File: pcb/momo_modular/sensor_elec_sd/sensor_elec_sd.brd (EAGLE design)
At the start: 100 x 33 mm, 27 parts, among them U1 AP7115-LDO, U2 16LF1847, U3 TS1100

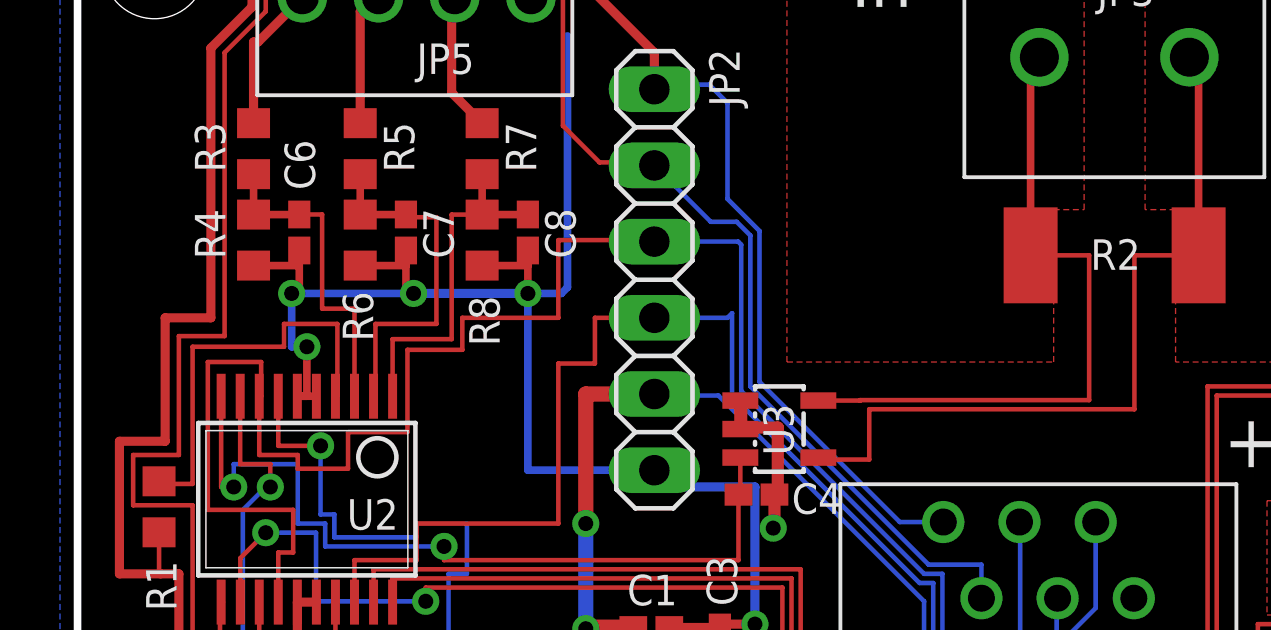
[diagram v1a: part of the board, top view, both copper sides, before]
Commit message: Final changes to sd card and voltage sensing board.
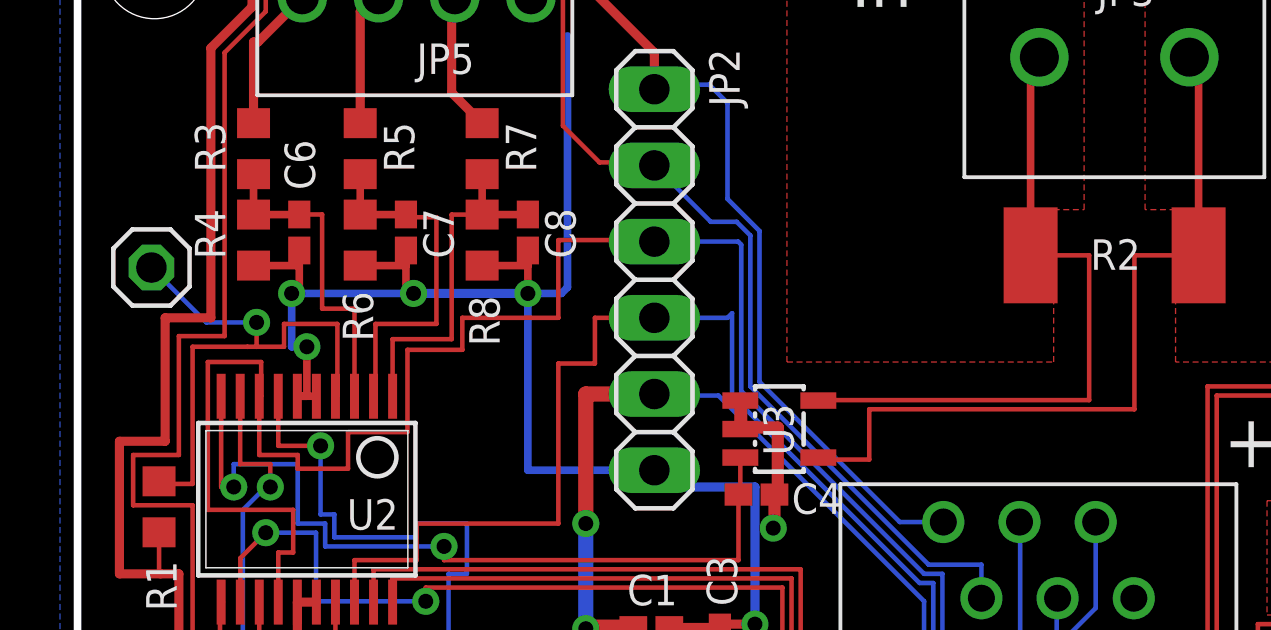
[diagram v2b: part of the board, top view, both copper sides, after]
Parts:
- added JP6: (no value), pinhead:1X01
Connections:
- net N$4: now also JP6.1
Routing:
- net N$4: track 14.1 -> 19.2 mm, vias 0 -> 1
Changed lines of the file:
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@@
 <attribute name="DIGIKEY-PN" value="A98335-ND" x="11.2776" y="33.2232" size="1.016" layer="27" display="off"/>
+</element>
+<element name="JP6" library="pinhead" package="1X01" value="" x="6.2484" y="24.2316" smashed="yes">
+<attribute name="VALUE" x="4.9784" y="21.0566" size="1.27" layer="27"/>
 </element>
 </elements>
@@
 <wire x1="12.446" y1="22.352" x2="10.668" y2="22.352" width="0.1524" layer="1"/>
 <wire x1="10.668" y1="22.352" x2="10.668" y2="21.59" width="0.1524" layer="1"/>
-<wire x1="10.668" y1="21.59" x2="7.62" y2="21.59" width="0.1524" layer="1"/>
+<wire x1="10.668" y1="21.59" x2="9.7536" y2="21.59" width="0.1524" layer="1"/>
+<wire x1="9.4488" y1="21.59" x2="7.62" y2="21.59" width="0.1524" layer="1"/>
 <wire x1="7.62" y1="21.59" x2="7.62" y2="17.018" width="0.1524" layer="1"/>
 <wire x1="7.62" y1="17.018" x2="6.35" y2="17.018" width="0.1524" layer="1"/>
 <wire x1="6.35" y1="17.018" x2="6.5024" y2="17.106" width="0.1524" layer="1"/>
+<contactref element="JP6" pad="1"/>
+<wire x1="6.2484" y1="24.2316" x2="8.0772" y2="22.4028" width="0.1524" layer="16"/>
+<wire x1="8.0772" y1="22.4028" x2="9.7536" y2="22.4028" width="0.1524" layer="16"/>
+<via x="9.7536" y="22.4028" extent="1-16" drill="0.5"/>
+<wire x1="9.7536" y1="22.4028" x2="9.7536" y2="21.59" width="0.1524" layer="1"/>
+<wire x1="9.7536" y1="21.59" x2="9.4488" y2="21.59" width="0.1524" layer="1"/>
 </signal>
 <signal name="SCL">
@@
 <contactref element="U3" pad="5"/>
 <wire x1="37.5056" y1="24.638" x2="35.554" y2="24.638" width="0.1524" layer="1"/>
-<wire x1="28.478" y1="19.7968" x2="29.8704" y2="19.7968" width="0.1524" layer="1"/>
-<wire x1="29.8704" y1="19.7968" x2="29.8704" y2="19.812" width="0.1524" layer="1"/>
-<wire x1="29.8704" y1="19.812" x2="37.5056" y2="19.812" width="0.1524" layer="1"/>
+<wire x1="28.478" y1="19.812" x2="37.5056" y2="19.812" width="0.1524" layer="1"/>
 <wire x1="37.5056" y1="19.812" x2="37.5056" y2="24.638" width="0.1524" layer="1"/>
+<wire x1="28.478" y1="19.812" x2="28.478" y2="19.7968" width="0.1524" layer="1"/>
 </signal>
 <signal name="ISENSE">

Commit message: Finished divider network spec'ing and standardized on 1% resistors to reduce BOM lines.
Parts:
- R3, R5: value (none) -> 620K 1%
- R4, R6, R8: value (none) -> 100K 1%
- R7: value (none) -> 806K 1%
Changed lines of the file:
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@@
 <attribute name="NAME" x="6.0706" y="14.4526" size="1.016" layer="25" rot="R270"/>
 <attribute name="VALUE" x="4.5974" y="16.891" size="1.27" layer="27" rot="R270"/>
-<attribute name="DIGIKEY-PN" value="P10KGCT-ND" x="6.5024" y="16.256" size="1.778" layer="27" rot="R270" display="off"/>
+<attribute name="DIGIKEY-PN" value="P10.0KHCT-ND" x="6.5024" y="16.256" size="1.778" layer="27" rot="R270" display="off"/>
 </element>
 <element name="JP2" library="components" package="1X06" value="MOMO-VERT-6M" x="23.0124" y="21.2852" smashed="yes" rot="R270">
@@
 <attribute name="NAME" x="39.2176" y="25.1714" size="1.016" layer="25" rot="R180"/>
 <attribute name="VALUE" x="40.894" y="27.813" size="1.27" layer="27" rot="R180"/>
-<attribute name="DIGKEY-PN" value="CRF2512-FV-R001ELFCT-ND" x="38.354" y="24.638" size="1.778" layer="27" rot="R180" display="off"/>
+<attribute name="DIGIKEY-PN" value="CRF2512-FV-R001ELFCT-ND" x="38.354" y="24.638" size="1.778" layer="27" rot="R180" display="off"/>
 </element>
 <element name="C4" library="rcl" package="C0402K" value="47 nF" x="26.416" y="16.6624" smashed="yes">
@@
 <attribute name="NAME" x="12.0582" y="11.0156" size="1.016" layer="25" rot="R270"/>
 <attribute name="VALUE" x="9.8784" y="11.168" size="1.016" layer="27" rot="R270"/>
-<attribute name="DIGKIEY-PN" value="445-1265-1-ND" x="11.3284" y="10.668" size="1.778" layer="27" rot="R270" display="off"/>
+<attribute name="DIGIKEY-PN" value="445-1265-1-ND" x="11.3284" y="10.668" size="1.778" layer="27" rot="R270" display="off"/>
 </element>
-<element name="R3" library="rcl" package="R0603" value="" x="9.652" y="28.194" smashed="yes" rot="R90">
+<element name="R3" library="rcl" package="R0603" value="620K 1%" x="9.652" y="28.194" smashed="yes" rot="R90">
 <attribute name="NAME" x="8.7122" y="27.4066" size="1.016" layer="25" rot="R90"/>
 <attribute name="VALUE" x="11.557" y="27.559" size="1.27" layer="27" rot="R90"/>
+<attribute name="DIGIKEY-PN" value="P620KHCT-ND" x="9.652" y="28.194" size="1.778" layer="27" rot="R90" display="off"/>
 </element>
-<element name="R4" library="rcl" package="R0603" value="" x="9.652" y="25.146" smashed="yes" rot="R90">
+<element name="R4" library="rcl" package="R0603" value="100K 1%" x="9.652" y="25.146" smashed="yes" rot="R90">
 <attribute name="NAME" x="8.7122" y="24.511" size="1.016" layer="25" rot="R90"/>
 <attribute name="VALUE" x="11.557" y="24.511" size="1.27" layer="27" rot="R90"/>
+<attribute name="DIGIKEY-PN" value="P100KHCT-ND" x="9.652" y="25.146" size="1.778" layer="27" rot="R90" display="off"/>
 </element>
-<element name="R5" library="rcl" package="R0603" value="" x="13.208" y="28.194" smashed="yes" rot="R90">
+<element name="R5" library="rcl" package="R0603" value="620K 1%" x="13.208" y="28.194" smashed="yes" rot="R90">
 <attribute name="NAME" x="15.0114" y="27.4066" size="1.016" layer="25" rot="R90"/>
 <attribute name="VALUE" x="15.113" y="27.559" size="1.27" layer="27" rot="R90"/>
+<attribute name="DIGIKEY-PN" value="P620KHCT-ND" x="13.208" y="28.194" size="1.778" layer="27" rot="R90" display="off"/>
 </element>
-<element name="R6" library="rcl" package="R0603" value="" x="13.208" y="25.146" smashed="yes" rot="R90">
+<element name="R6" library="rcl" package="R0603" value="100K 1%" x="13.208" y="25.146" smashed="yes" rot="R90">
 <attribute name="NAME" x="13.6398" y="21.7678" size="1.016" layer="25" rot="R90"/>
 <attribute name="VALUE" x="15.113" y="24.511" size="1.27" layer="27" rot="R90"/>
+<attribute name="DIGIKEY-PN" value="P100KHCT-ND" x="13.208" y="25.146" size="1.778" layer="27" rot="R90" display="off"/>
 </element>
-<element name="R7" library="rcl" package="R0603" value="" x="17.272" y="28.194" smashed="yes" rot="R90">
+<element name="R7" library="rcl" package="R0603" value="806K 1%" x="17.272" y="28.194" smashed="yes" rot="R90">
 <attribute name="NAME" x="19.0754" y="27.4066" size="1.016" layer="25" rot="R90"/>
 <attribute name="VALUE" x="19.177" y="27.559" size="1.27" layer="27" rot="R90"/>
+<attribute name="DIGIKEY-PN" value="P806KHCT-ND" x="17.272" y="28.194" size="1.778" layer="27" rot="R90" display="off"/>
 </element>
-<element name="R8" library="rcl" package="R0603" value="" x="17.272" y="25.146" smashed="yes" rot="R90">
+<element name="R8" library="rcl" package="R0603" value="100K 1%" x="17.272" y="25.146" smashed="yes" rot="R90">
 <attribute name="NAME" x="17.8562" y="21.6154" size="1.016" layer="25" rot="R90"/>
 <attribute name="VALUE" x="19.177" y="24.511" size="1.27" layer="27" rot="R90"/>
+<attribute name="DIGIKEY-PN" value="P100KHCT-ND" x="17.272" y="25.146" size="1.778" layer="27" rot="R90" display="off"/>
 </element>
 <element name="C6" library="rcl" package="C0402K" value="100 nF" x="11.176" y="25.4" smashed="yes" rot="R270">
@@
 <attribute name="NAME" x="21.4122" y="8.2042" size="1.016" layer="25" rot="R180"/>
 <attribute name="VALUE" x="24.003" y="9.6774" size="1.27" layer="27" rot="R180"/>
-<attribute name="DIGIKEY-PN" value="P100KGCT-ND" x="23.368" y="7.7724" size="1.778" layer="27" rot="R180" display="off"/>
+<attribute name="DIGIKEY-PN" value="P100KHCT-ND" x="23.368" y="7.7724" size="1.778" layer="27" rot="R180" display="off"/>
 </element>
 <element name="C9" library="rcl" package="C1206K" value="22 uF" x="44.6532" y="17.0688" smashed="yes" rot="R270">
